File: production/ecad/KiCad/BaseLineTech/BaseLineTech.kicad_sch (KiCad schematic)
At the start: 0 parts

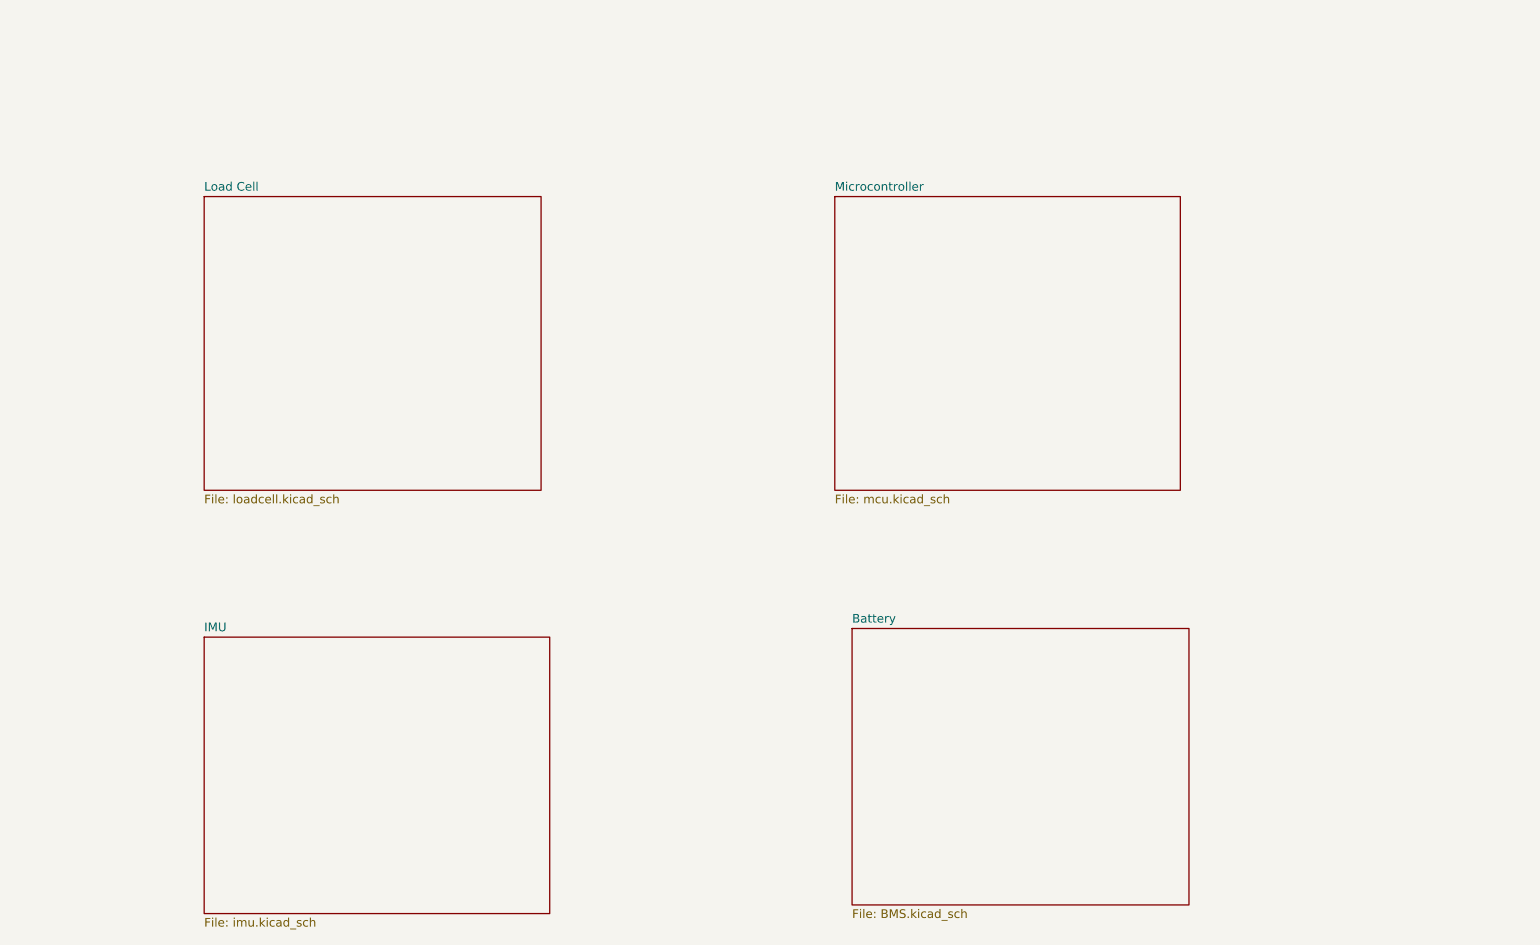
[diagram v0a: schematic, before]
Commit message: add motor schematic sheet
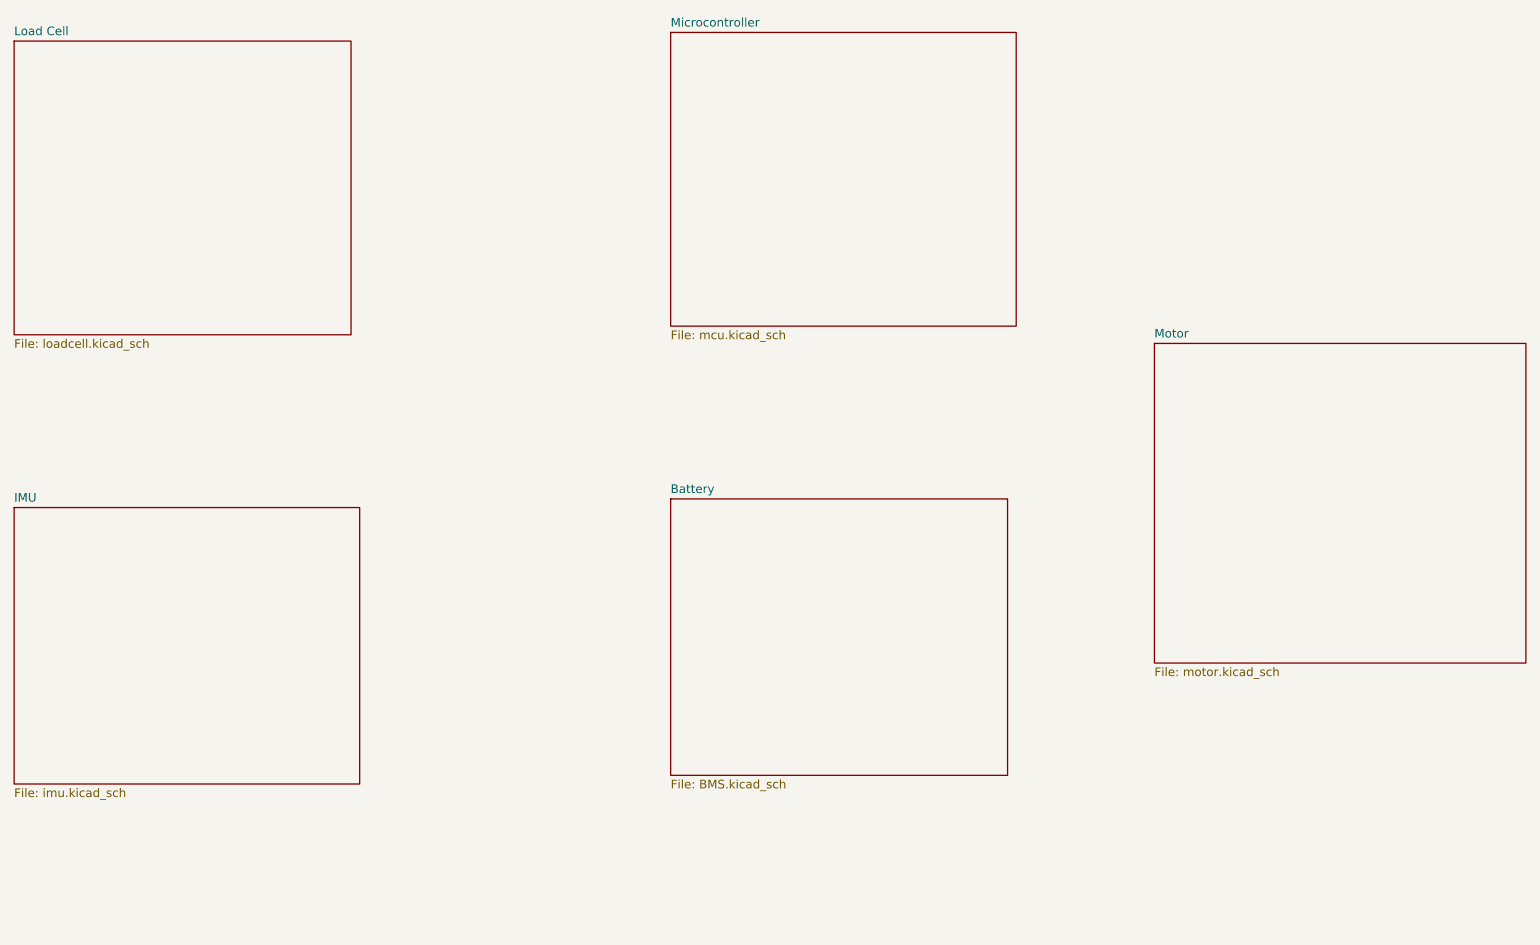
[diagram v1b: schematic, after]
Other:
- added sheet Motor (motor.kicad_sch)
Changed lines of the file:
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@@
 (kicad_sch (version 20230121) (generator eeschema)
   (paper "A4")
-  (sheet (at 162.56 116.84) (size 49.53 40.64) (fields_autoplaced)
+  (sheet (at 135.89 97.79) (size 49.53 40.64) (fields_autoplaced)
     (stroke (width 0.1524) (type solid))
     (fill (color 0 0 0 0.0000))
-    (property "Sheetname" "Battery " (at 162.56 116.1284 0)
+    (property "Sheetname" "Battery " (at 135.89 97.0784 0)
       (effects (font (size 1.27 1.27)) (justify left bottom))
     )
-    (property "Sheetfile" "BMS.kicad_sch" (at 162.56 158.0646 0)
+    (property "Sheetfile" "BMS.kicad_sch" (at 135.89 139.0146 0)
       (effects (font (size 1.27 1.27)) (justify left top))
     )
@@
     )
   )
-  (sheet (at 160.02 53.34) (size 50.8 43.18) (fields_autoplaced)
+  (sheet (at 135.89 29.21) (size 50.8 43.18) (fields_autoplaced)
     (stroke (width 0.1524) (type solid))
     (fill (color 0 0 0 0.0000))
-    (property "Sheetname" "Microcontroller" (at 160.02 52.6284 0)
+    (property "Sheetname" "Microcontroller" (at 135.89 28.4984 0)
       (effects (font (size 1.27 1.27)) (justify left bottom))
     )
-    (property "Sheetfile" "mcu.kicad_sch" (at 160.02 97.1046 0)
+    (property "Sheetfile" "mcu.kicad_sch" (at 135.89 72.9746 0)
       (effects (font (size 1.27 1.27)) (justify left top))
     )
@@
     )
   )
-  (sheet (at 67.31 118.11) (size 50.8 40.64) (fields_autoplaced)
+  (sheet (at 39.37 99.06) (size 50.8 40.64) (fields_autoplaced)
     (stroke (width 0.1524) (type solid))
     (fill (color 0 0 0 0.0000))
-    (property "Sheetname" "IMU" (at 67.31 117.3984 0)
+    (property "Sheetname" "IMU" (at 39.37 98.3484 0)
       (effects (font (size 1.27 1.27)) (justify left bottom))
     )
-    (property "Sheetfile" "imu.kicad_sch" (at 67.31 159.3346 0)
+    (property "Sheetfile" "imu.kicad_sch" (at 39.37 140.2846 0)
       (effects (font (size 1.27 1.27)) (justify left top))
     )
@@
     )
   )
-  (sheet (at 67.31 53.34) (size 49.53 43.18) (fields_autoplaced)
+  (sheet (at 39.37 30.48) (size 49.53 43.18) (fields_autoplaced)
     (stroke (width 0.1524) (type solid))
     (fill (color 0 0 0 0.0000))
-    (property "Sheetname" "Load Cell" (at 67.31 52.6284 0)
+    (property "Sheetname" "Load Cell" (at 39.37 29.7684 0)
       (effects (font (size 1.27 1.27)) (justify left bottom))
     )
-    (property "Sheetfile" "loadcell.kicad_sch" (at 67.31 97.1046 0)
+    (property "Sheetfile" "loadcell.kicad_sch" (at 39.37 74.2446 0)
       (effects (font (size 1.27 1.27)) (justify left top))
     )
@@
       )
     )
+  )
+  (sheet (at 207.01 74.93) (size 54.61 46.99) (fields_autoplaced)
+    (stroke (width 0.1524) (type solid))
+    (fill (color 0 0 0 0.0000))
+    (property "Sheetname" "Motor" (at 207.01 74.2184 0)
+      (effects (font (size 1.27 1.27)) (justify left bottom))
+    )
+    (property "Sheetfile" "motor.kicad_sch" (at 207.01 122.5046 0)
+      (effects (font (size 1.27 1.27)) (justify left top))
+    )
+    (instances
+      (project "BaseLineTech"
+        (path "/d7630117-0ace-4af2-a4d3-7d7246262c19" (page "6"))
+      )
+    )
